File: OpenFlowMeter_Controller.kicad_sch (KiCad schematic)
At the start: 12 parts, among them J3 Conn_01x06, J5 Conn_01x03, U2 STM32F103C8Tx, U5 SN65HVD231, Y1 12 MHz

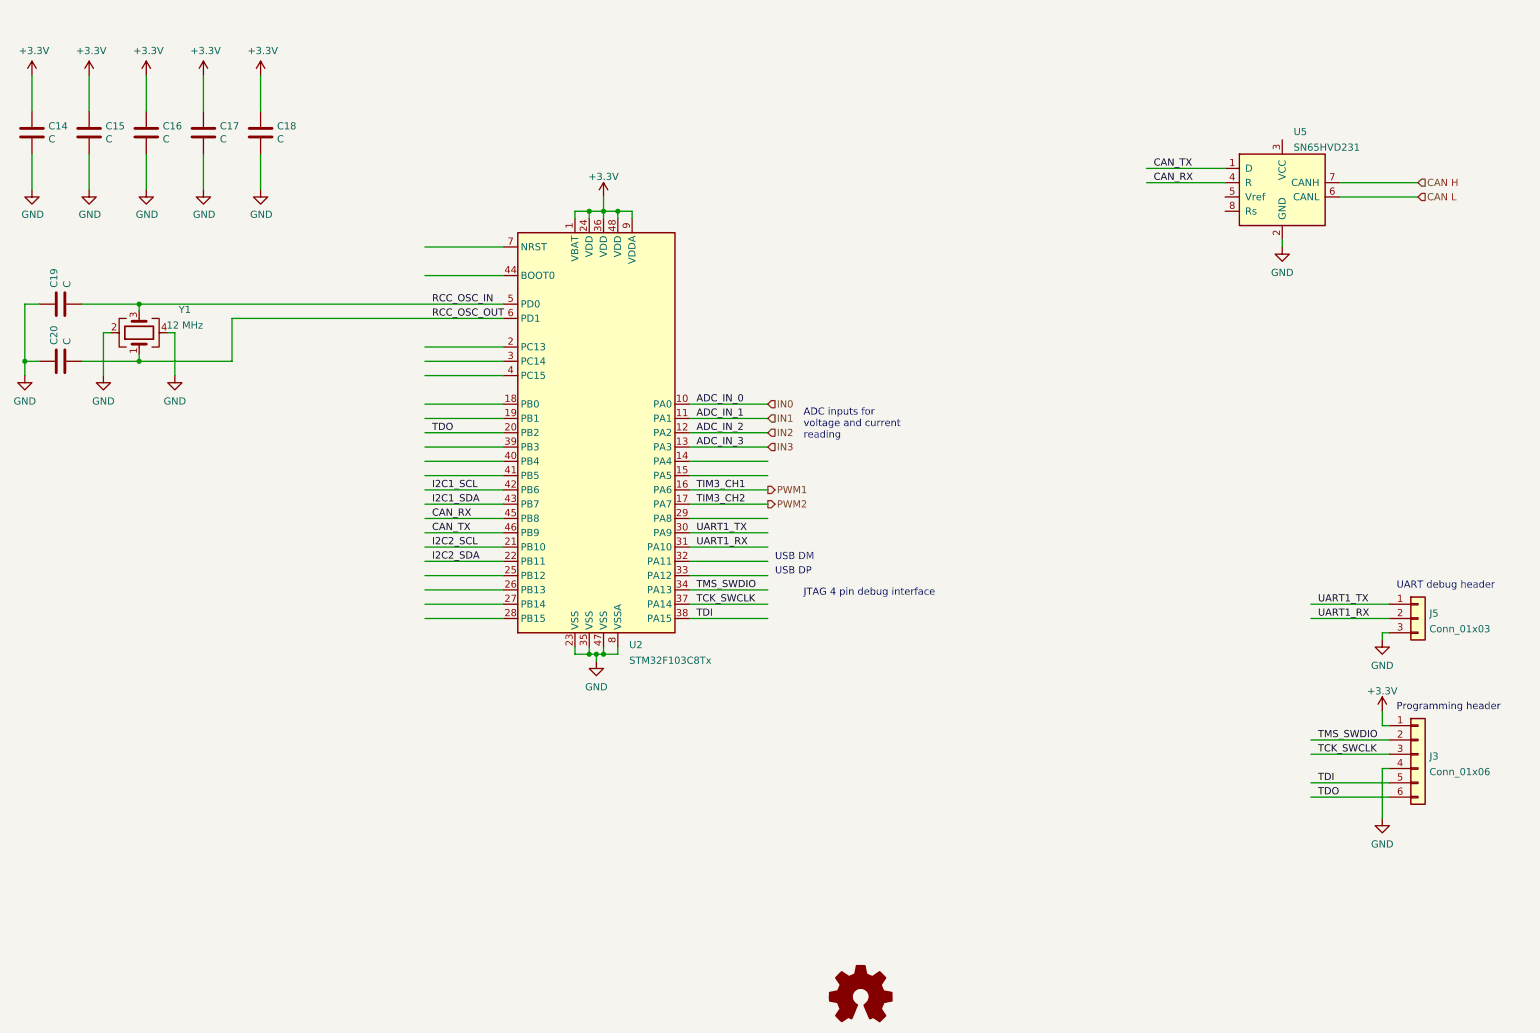
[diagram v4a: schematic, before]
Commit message: added LEDs and further routing
Added 4 LEDs, which can display the status
partially done routing of LEDs
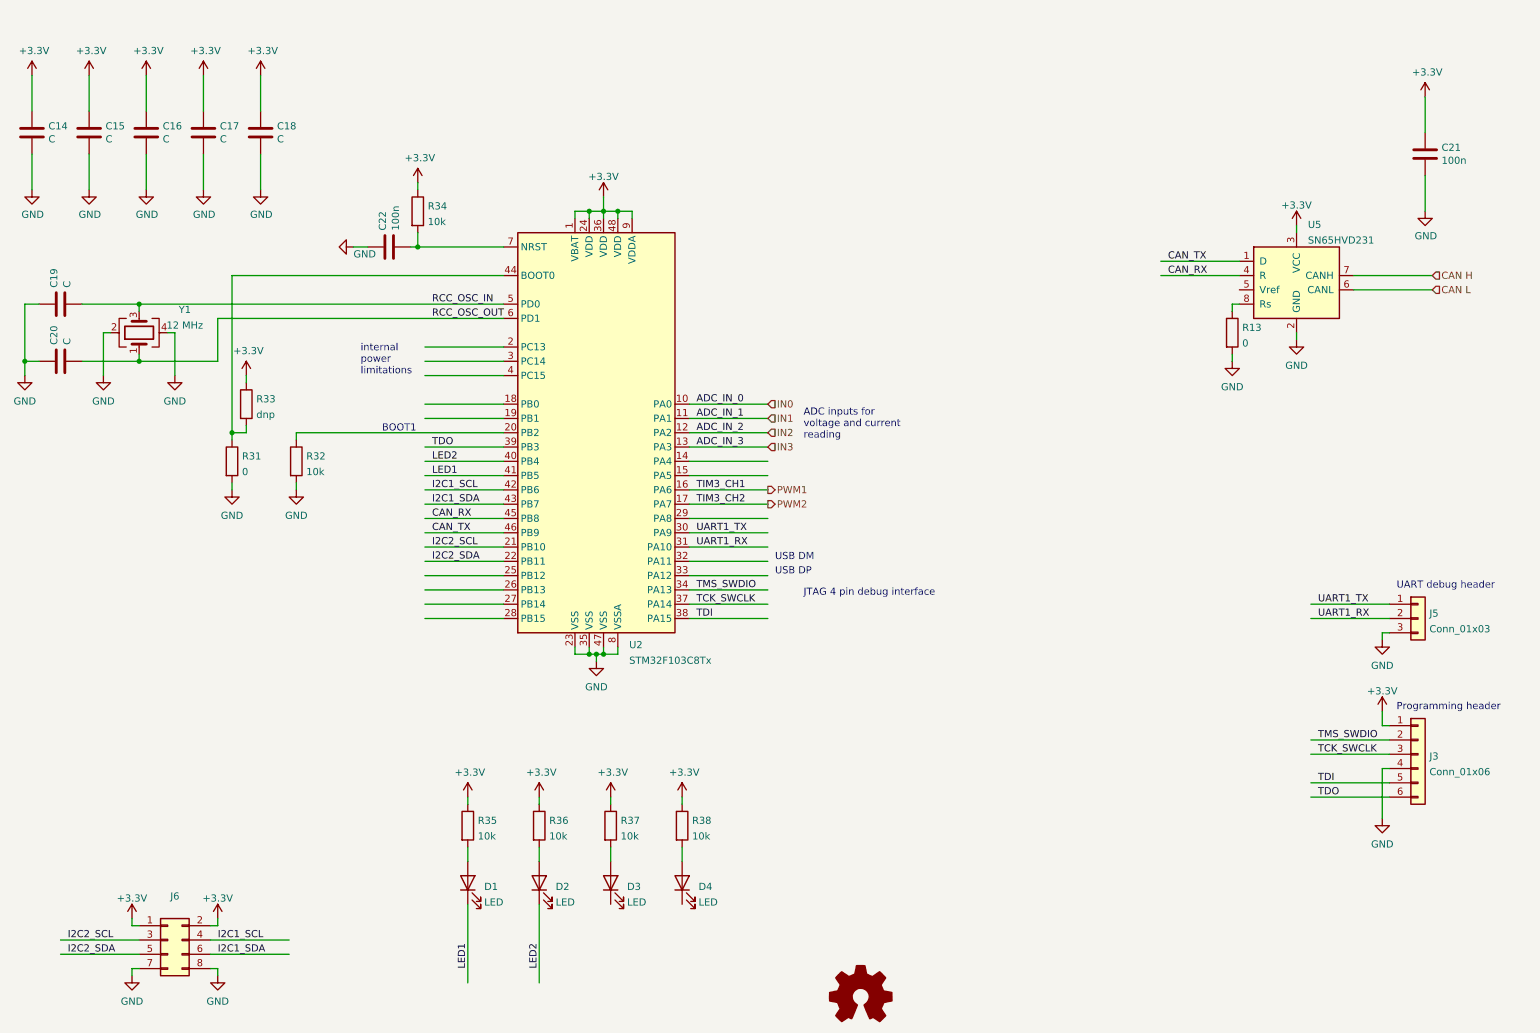
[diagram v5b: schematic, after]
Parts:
- added C21, C22: 100n, Capacitor_SMD:C_0603_1608Metric_Pad1.08x0.95mm_HandSolder, symbol Device:C
- added D1, D2, D3, D4: LED, LED_SMD:LED_0603_1608Metric_Pad1.05x0.95mm_HandSolder, symbol Device:LED
- added J6: Conn_02x04_Odd_Even, Connector_PinHeader_2.54mm:PinHeader_2x04_P2.54mm_Vertical_SMD, symbol Connector_Generic:Conn_02x04_Odd_Even
- added R13, R31: 0, Resistor_SMD:R_0603_1608Metric_Pad0.98x0.95mm_HandSolder, symbol Device:R
- added R32, R34, R35, R36, R37, R38: 10k, Resistor_SMD:R_0603_1608Metric_Pad0.98x0.95mm_HandSolder, symbol Device:R
- added R33: dnp, Resistor_SMD:R_0603_1608Metric_Pad0.98x0.95mm_HandSolder, symbol Device:R
- Y1: footprint Crystal:Crystal_SMD_EuroQuartz_MT-4Pin_3.2x2.5mm_HandSoldering -> Crystal:Crystal_SMD_EuroQuartz_MT-4Pin_3.2x2.5mm
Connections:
- net +3V3: now also U5.3 (VCC), C21.1, J6.1 (Pin_1), J6.2 (Pin_2), R33.1, R34.1, R35.1, R36.1, R37.1, R38.1
- net GND: now also C21.2, C22.1, J6.7 (Pin_7), J6.8 (Pin_8), R13.2, R31.2, R32.2
- net I2C1_SCL: now also J6.4 (Pin_4)
- net I2C1_SDA: now also J6.6 (Pin_6)
- net I2C2_SCL: now also J6.3 (Pin_3)
- net I2C2_SDA: now also J6.5 (Pin_5)
- net TDO: now also U2.39 (PB3); no longer U2.20 (PB2)
- net LED2: now reaches U2.40 (PB4)
- net LED2: now also D2.1 (K)
- net LED1: now reaches U2.41 (PB5)
- net LED1: now also D1.1 (K)
- net at U2.44 (BOOT0): now also R31.1, R33.2
- net at U2.7 (NRST): now also C22.2, R34.2
- net at U5.8 (Rs): now also R13.1
- new net: D1.2 (A), R35.2
- new net: R32.1, U2.20 (PB2)
- new net: D2.2 (A), R36.2
- new net: D3.2 (A), R37.2
- new net: D4.2 (A), R38.2
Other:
- note added: "BOOT1"
- note added: "internal power limitations"
- moved on the sheet: U5

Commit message: BUGFIX footprint of LT1490
Footprint of LT1490 is SOIC8 and not Micro 8 -> had to enlarge the board.
At the same step, changed all footprints from handsolder to normal solder. (saves a little space)
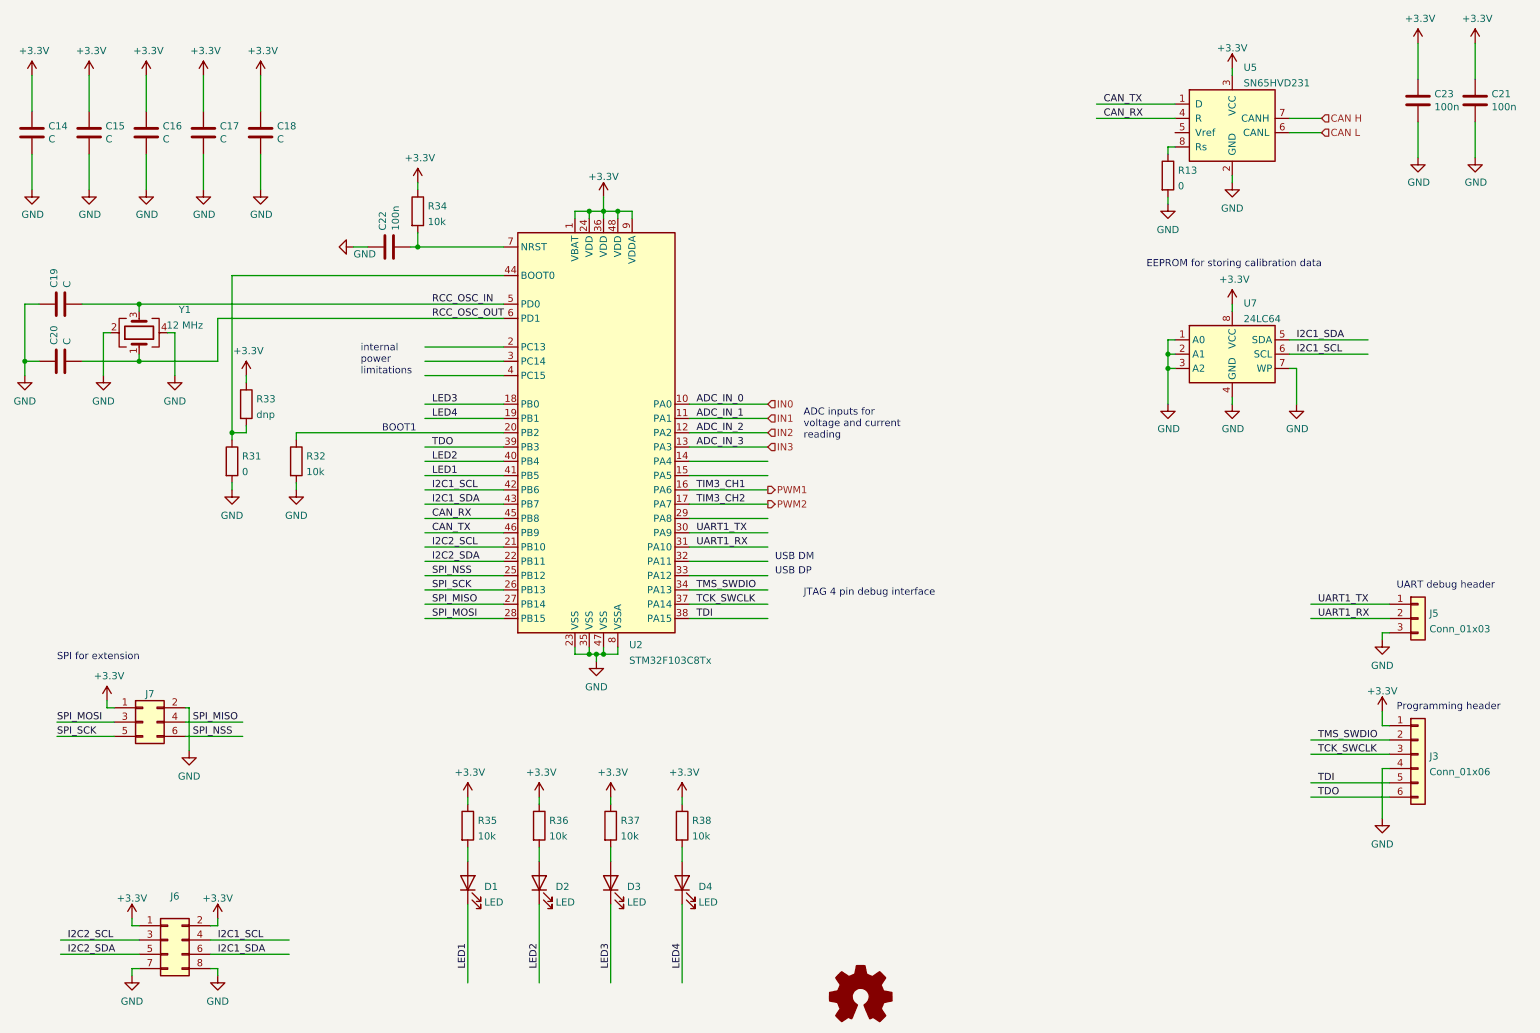
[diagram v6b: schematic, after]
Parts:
- added C23: 100n, Capacitor_SMD:C_0603_1608Metric, symbol Device:C
- added J7: Conn_02x03_Odd_Even, Connector_PinHeader_2.54mm:PinHeader_2x03_P2.54mm_Vertical_SMD, symbol Connector_Generic:Conn_02x03_Odd_Even
- added U7: 24LC64, Package_DIP:DIP-8_W7.62mm, symbol Memory_EEPROM:24LC64
- C14, C15, C16, C17, C18, C19, C20, C21, C22: footprint Capacitor_SMD:C_0603_1608Metric_Pad1.08x0.95mm_HandSolder -> Capacitor_SMD:C_0603_1608Metric
- D1, D2, D3, D4: footprint LED_SMD:LED_0603_1608Metric_Pad1.05x0.95mm_HandSolder -> LED_SMD:LED_0603_1608Metric
- R13, R31, R32, R33, R34, R35, R36, R37, R38: footprint Resistor_SMD:R_0603_1608Metric_Pad0.98x0.95mm_HandSolder -> Resistor_SMD:R_0603_1608Metric
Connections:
- net +3V3: now also C23.1, J7.1 (Pin_1), U7.8 (VCC)
- net GND: now also C23.2, J7.2 (Pin_2), U7.1 (A0), U7.2 (A1), U7.3 (A2), U7.4 (GND), U7.7 (WP)
- net I2C1_SCL: now also U7.6 (SCL)
- net I2C1_SDA: now also U7.5 (SDA)
- net LED3: now reaches D3.1 (K)
- net LED3: now also U2.18 (PB0)
- net LED4: now reaches U2.19 (PB1)
- net LED4: now also D4.1 (K)
- net SPI_NSS: now reaches U2.25 (PB12)
- net SPI_NSS: now also J7.6 (Pin_6)
- net SPI_SCK: now reaches U2.26 (PB13)
- net SPI_SCK: now also J7.5 (Pin_5)
- net SPI_MISO: now reaches U2.27 (PB14)
- net SPI_MISO: now also J7.4 (Pin_4)
- net SPI_MOSI: now reaches U2.28 (PB15)
- net SPI_MOSI: now also J7.3 (Pin_3)
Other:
- note added: "EEPROM for storing calibration data"
- note added: "SPI for extension"
- moved on the sheet: C21, R13, U5
